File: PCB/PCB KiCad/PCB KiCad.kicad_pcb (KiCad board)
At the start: 2 copper layers, 80 x 120 mm, 0 parts

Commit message: start of component placement
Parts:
- added A1: Arduino_UNO_R3, Module:Arduino_UNO_R3, F.Cu at (71.8, 40.0)
- added C1: 100n, Capacitor_SMD:C_0805_2012Metric_Pad1.18x1.45mm_HandSolder, F.Cu at (178.0, 149.0)
- added C10: 18p, Capacitor_SMD:C_0805_2012Metric_Pad1.18x1.45mm_HandSolder, F.Cu at (64.0, 104.0)
- added C11: 10u, Capacitor_SMD:C_0805_2012Metric_Pad1.18x1.45mm_HandSolder, F.Cu at (137.0, 87.0)
- added C12: 22u, Capacitor_SMD:C_0805_2012Metric_Pad1.18x1.45mm_HandSolder, F.Cu at (134.0, 104.0)
- added C13: 100n, Capacitor_SMD:C_0805_2012Metric_Pad1.18x1.45mm_HandSolder, F.Cu at (135.0, 119.0)
- added C14: 100n, Capacitor_SMD:C_0805_2012Metric_Pad1.18x1.45mm_HandSolder, F.Cu at (136.0, 94.0)
- added C15: 100n, Capacitor_SMD:C_0805_2012Metric_Pad1.18x1.45mm_HandSolder, F.Cu at (127.0, 100.0)
- added C16: 22u, Capacitor_SMD:C_0805_2012Metric_Pad1.18x1.45mm_HandSolder, F.Cu at (127.0, 105.0)
- added C17: 100n, Capacitor_SMD:C_0805_2012Metric_Pad1.18x1.45mm_HandSolder, F.Cu at (128.0, 143.0)
- added C2: 51p, Capacitor_SMD:C_0805_2012Metric_Pad1.18x1.45mm_HandSolder, F.Cu at (196.0, 146.0)
- added C3: 51p, Capacitor_SMD:C_0805_2012Metric_Pad1.18x1.45mm_HandSolder, F.Cu at (163.0, 149.0)
- added C4: 47n, Capacitor_SMD:C_0805_2012Metric_Pad1.18x1.45mm_HandSolder, F.Cu at (171.0, 142.0)
- added C5: 100p, Capacitor_SMD:C_0805_2012Metric_Pad1.18x1.45mm_HandSolder, F.Cu at (164.0, 141.0)
- added C6: 22u, Capacitor_SMD:C_0805_2012Metric_Pad1.18x1.45mm_HandSolder, F.Cu at (199.1, 116.0)
- added C7: 100n, Capacitor_SMD:C_0805_2012Metric_Pad1.18x1.45mm_HandSolder, F.Cu at (206.0, 114.0)
- added C8: 100p, Capacitor_SMD:C_0805_2012Metric_Pad1.18x1.45mm_HandSolder, F.Cu at (215.0, 116.0)
- added C9: 18p, Capacitor_SMD:C_0805_2012Metric_Pad1.18x1.45mm_HandSolder, F.Cu at (64.0, 110.0)
- added D1: 0090-3111-185, Diode_SMD:D_1206_3216Metric_Pad1.42x1.75mm_HandSolder, F.Cu at (83.0, 161.0)
- added D10: LED, LED_SMD:LED_1206_3216Metric_Pad1.42x1.75mm_HandSolder, F.Cu at (72.5, 159.0)
- added D11: LED, LED_SMD:LED_1206_3216Metric_Pad1.42x1.75mm_HandSolder, F.Cu at (76.0, 153.0)
- added D2: LED BLUE, LED_SMD:LED_0805_2012Metric_Pad1.15x1.40mm_HandSolder, F.Cu at (79.0, 31.0)
- added D3: LED RED, LED_SMD:LED_0805_2012Metric_Pad1.15x1.40mm_HandSolder, F.Cu at (90.0, 31.0)
- added D4: LED, LED_SMD:LED_1206_3216Metric_Pad1.42x1.75mm_HandSolder, F.Cu at (90.0, 153.0)
- added D5: LED, LED_SMD:LED_1206_3216Metric_Pad1.42x1.75mm_HandSolder, F.Cu at (90.0, 159.0)
- added D6: LED, LED_SMD:LED_1206_3216Metric_Pad1.42x1.75mm_HandSolder, F.Cu at (90.0, 165.0)
- added D7: LED, LED_SMD:LED_1206_3216Metric_Pad1.42x1.75mm_HandSolder, F.Cu at (88.5, 171.0)
- added D8: LED, LED_SMD:LED_1206_3216Metric_Pad1.42x1.75mm_HandSolder, F.Cu at (74.0, 171.0)
- added D9: LED, LED_SMD:LED_1206_3216Metric_Pad1.42x1.75mm_HandSolder, F.Cu at (73.0, 165.0)
- added FB1: FerriteBead, Resistor_SMD:R_0805_2012Metric_Pad1.20x1.40mm_HandSolder, F.Cu at (128.0, 92.0)
- added J1: ADC Debug, Connector_PinHeader_2.54mm:PinHeader_1x08_P2.54mm_Vertical, F.Cu at (45.0, 101.1)
- added J2: LED Debug, Connector_PinHeader_2.54mm:PinHeader_1x04_P2.54mm_Vertical, F.Cu at (120.0, 137.0)
- added R1: 240k, Resistor_SMD:R_0805_2012Metric_Pad1.20x1.40mm_HandSolder, F.Cu at (187.0, 137.0)
- added R10: 100, Resistor_SMD:R_0805_2012Metric_Pad1.20x1.40mm_HandSolder, F.Cu at (82.7, 95.0)
- added R11: 0, Resistor_SMD:R_0805_2012Metric_Pad1.20x1.40mm_HandSolder, F.Cu at (77.3, 95.0)
- added R12: 100, Resistor_SMD:R_0805_2012Metric_Pad1.20x1.40mm_HandSolder, F.Cu at (88.1, 95.0)
- added R13: 0, Resistor_SMD:R_0805_2012Metric_Pad1.20x1.40mm_HandSolder, F.Cu at (99.0, 95.0)
- added R14: 100, Resistor_SMD:R_0805_2012Metric_Pad1.20x1.40mm_HandSolder, F.Cu at (93.6, 95.0)
- added R15: 100, Resistor_SMD:R_0805_2012Metric_Pad1.20x1.40mm_HandSolder, F.Cu at (92.0, 100.0)
- added R16: 100, Resistor_SMD:R_0805_2012Metric_Pad1.20x1.40mm_HandSolder, F.Cu at (78.0, 35.0)
- added R17: 82, Resistor_SMD:R_0805_2012Metric_Pad1.20x1.40mm_HandSolder, F.Cu at (90.0, 35.0)
- added R18: 10k, Resistor_SMD:R_0805_2012Metric_Pad1.20x1.40mm_HandSolder, F.Cu at (60.0, 23.0)
- added R19: 10k, Resistor_SMD:R_0805_2012Metric_Pad1.20x1.40mm_HandSolder, F.Cu at (73.0, 23.0)
- added R2: 240k, Resistor_SMD:R_0805_2012Metric_Pad1.20x1.40mm_HandSolder, F.Cu at (171.0, 152.0)
- added R20: 1k, Resistor_SMD:R_0805_2012Metric_Pad1.20x1.40mm_HandSolder, F.Cu at (129.0, 120.0)
- added R21: 0, Resistor_SMD:R_0805_2012Metric_Pad1.20x1.40mm_HandSolder, F.Cu at (105.0, 95.0)
- added R22: 0, Resistor_SMD:R_0805_2012Metric_Pad1.20x1.40mm_HandSolder, F.Cu at (110.0, 92.0)
- added R23: 0, Resistor_SMD:R_0805_2012Metric_Pad1.20x1.40mm_HandSolder, F.Cu at (101.0, 102.0)
- added R24: 1k, Resistor_SMD:R_0805_2012Metric_Pad1.20x1.40mm_HandSolder, F.Cu at (127.0, 149.0)
- added R25: 56, Resistor_SMD:R_0805_2012Metric_Pad1.20x1.40mm_HandSolder, F.Cu at (98.0, 153.0)
- added R26: 62, Resistor_SMD:R_0805_2012Metric_Pad1.20x1.40mm_HandSolder, F.Cu at (98.0, 159.0)
- added R27: 70, Resistor_SMD:R_0805_2012Metric_Pad1.20x1.40mm_HandSolder, F.Cu at (98.0, 165.0)
- added R28: 75, Resistor_SMD:R_0805_2012Metric_Pad1.20x1.40mm_HandSolder, F.Cu at (98.0, 171.0)
- added R29: 75, Resistor_SMD:R_0805_2012Metric_Pad1.20x1.40mm_HandSolder, F.Cu at (65.0, 171.0)
- added R3: 301, Resistor_SMD:R_0805_2012Metric_Pad1.20x1.40mm_HandSolder, F.Cu at (179.0, 139.0)
- added R30: 75, Resistor_SMD:R_0805_2012Metric_Pad1.20x1.40mm_HandSolder, F.Cu at (63.0, 165.0)
- added R31: 75, Resistor_SMD:R_0805_2012Metric_Pad1.20x1.40mm_HandSolder, F.Cu at (63.0, 159.0)
- added R32: 82, Resistor_SMD:R_0805_2012Metric_Pad1.20x1.40mm_HandSolder, F.Cu at (64.0, 153.0)
- added R4: 301, Resistor_SMD:R_0805_2012Metric_Pad1.20x1.40mm_HandSolder, F.Cu at (188.0, 147.0)
- added R5: 49.9, Resistor_SMD:R_0805_2012Metric_Pad1.20x1.40mm_HandSolder, F.Cu at (191.0, 115.0)
- added R6: 49.9, Resistor_SMD:R_0805_2012Metric_Pad1.20x1.40mm_HandSolder, F.Cu at (192.0, 121.0)
- added R7: 10k, Resistor_SMD:R_0805_2012Metric_Pad1.20x1.40mm_HandSolder, F.Cu at (61.0, 95.0)
- added R8: 10k, Resistor_SMD:R_0805_2012Metric_Pad1.20x1.40mm_HandSolder, F.Cu at (66.4, 95.0)
- added R9: 100, Resistor_SMD:R_0805_2012Metric_Pad1.20x1.40mm_HandSolder, F.Cu at (71.9, 95.0)
- added SW1: MCU_RESET, Button_Switch_THT:SW_PUSH_6mm_H4.3mm, F.Cu at (52.8, 29.8)
- added SW2: TRIGGER, Button_Switch_THT:SW_PUSH_6mm_H4.3mm, F.Cu at (63.8, 29.8)
- added U2: ADS1256IDBT, ADS1256:Texas_Instruments-ADS1256IDBT-Level_A, F.Cu at (176.5, 126.6)
- added U3: LM285D-2.5, Package_SO:SOIC-8_3.9x4.9mm_P1.27mm, F.Cu at (114.0, 121.0)
- added U4: AMS1117-3.3, Package_TO_SOT_SMD:SOT-223-3_TabPin2, F.Cu at (115.0, 102.0)
- added U5: TLC59208FIPWR, TLC59208:Texas_Instruments-TLC59208FIPWR-Level_A, F.Cu at (108.0, 142.0)
- added Y1: 7.68MHz, Crystal:Crystal_HC49-U_Vertical, F.Cu at (55.0, 110.0)

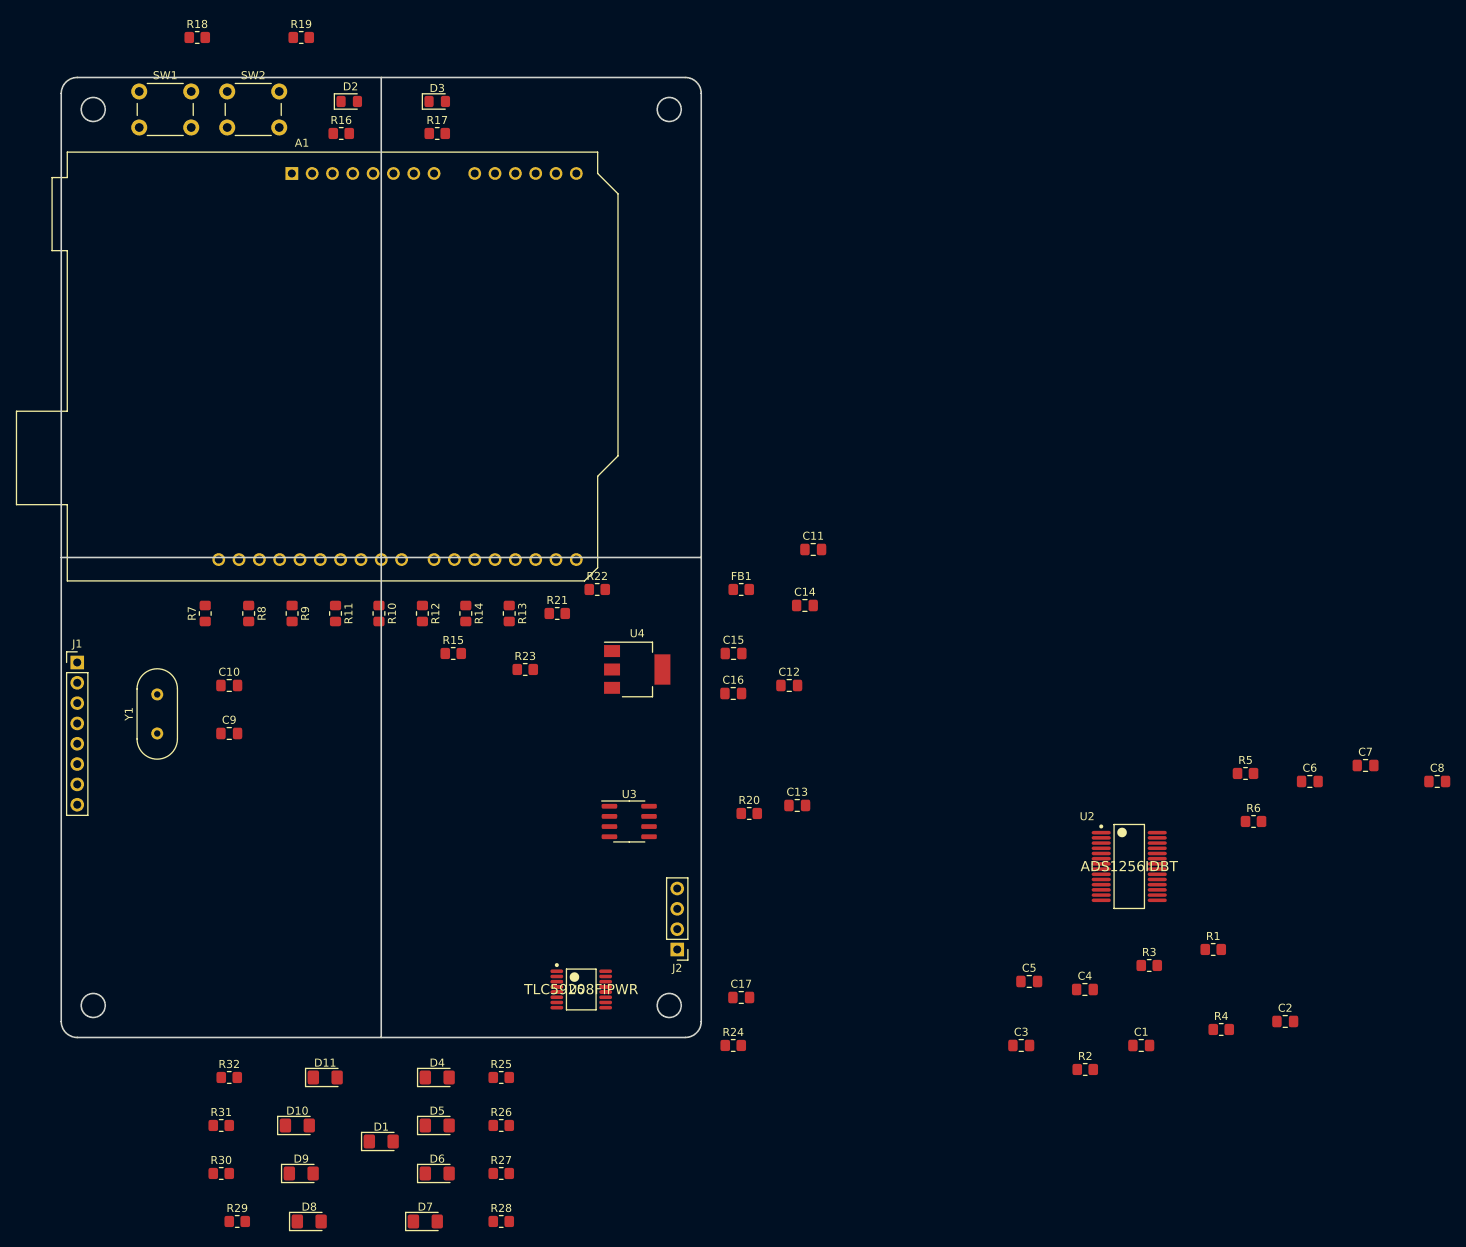
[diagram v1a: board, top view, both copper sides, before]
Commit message: placement of components
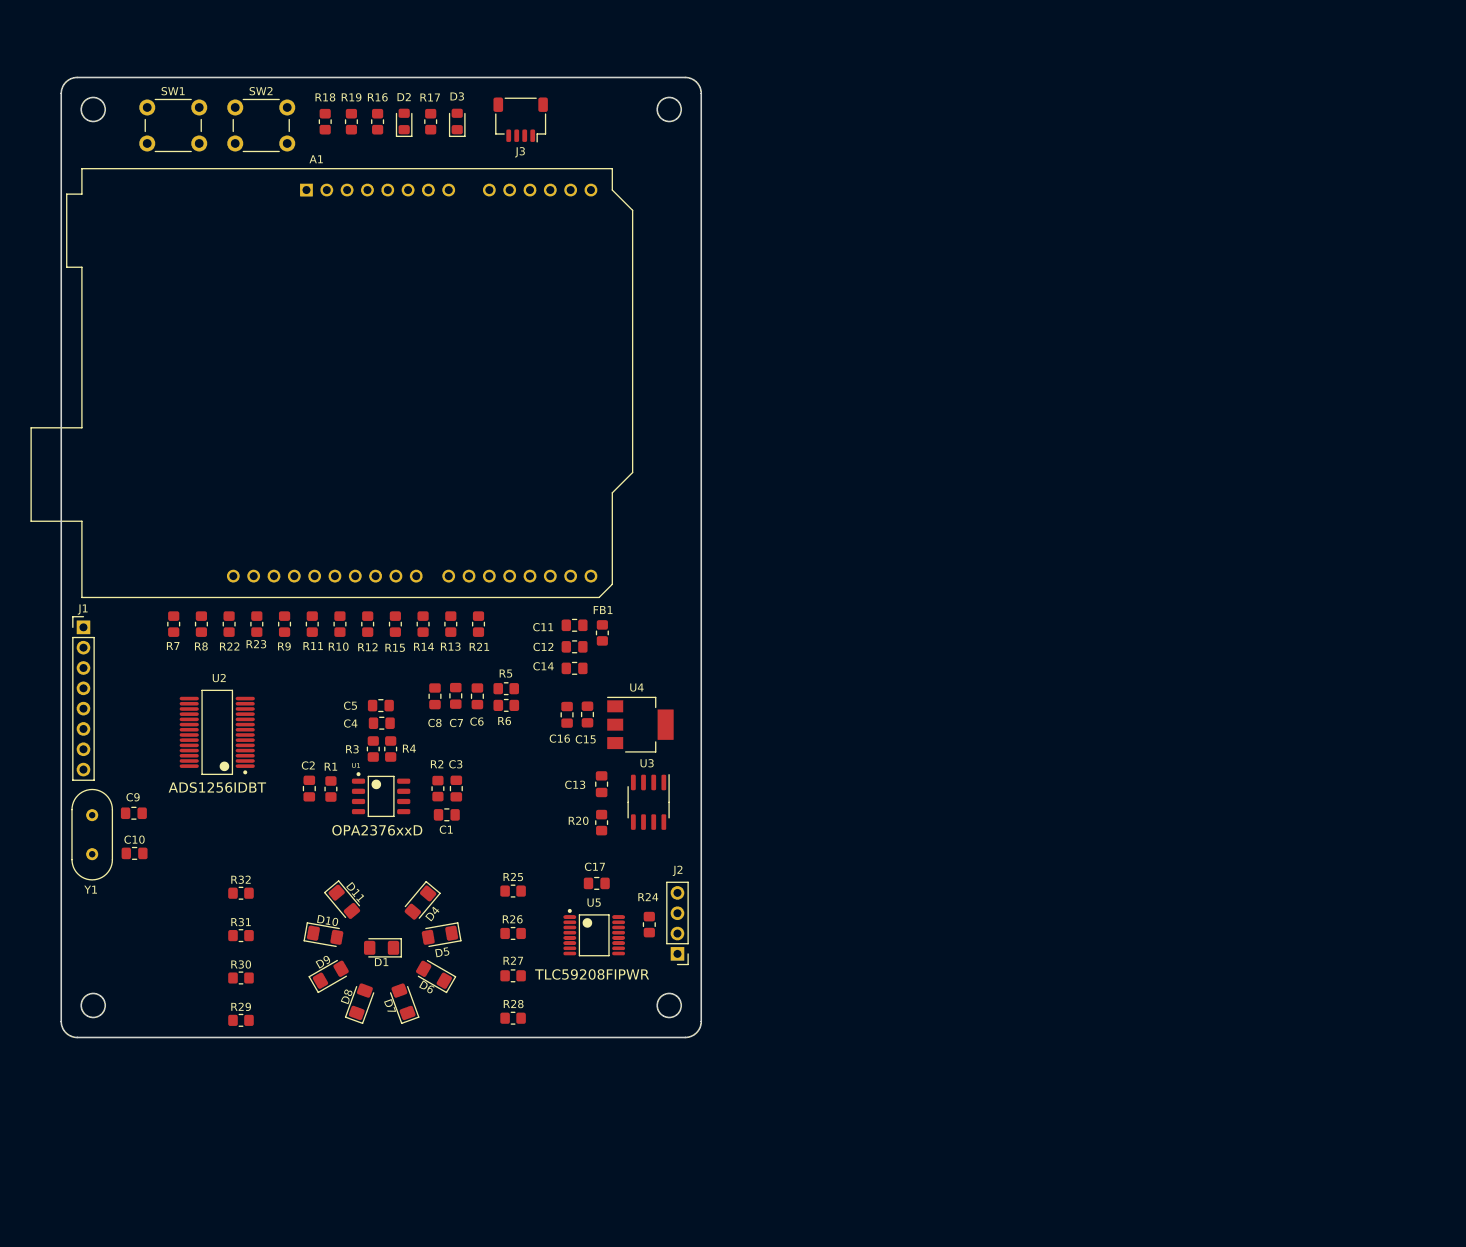
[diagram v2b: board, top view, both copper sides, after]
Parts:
- added J3: Qwiic, Connector_JST:JST_SH_SM04B-SRSS-TB_1x04-1MP_P1.00mm_Horizontal, F.Cu at (100.4, 33.3)
- added U1: OPA2376xxD, eec:Texas_Instruments-OPA2376AID-Level_A, F.Cu at (83.0, 117.9)
- SW1, SW2: footprint Button_Switch_THT:SW_PUSH_6mm_H4.3mm -> Button_Switch_THT:SW_PUSH_6mm
- moved C8 125.7 mm to (89.7, 105.3), turned to -90 degrees
- moved C2 125.4 mm to (74.0, 116.9), turned to 90 degrees
- moved U2 115.2 mm to (62.5, 109.9), turned to 180 degrees
- moved C7 114.0 mm to (92.3, 105.3), turned to -90 degrees
- moved R1 112.1 mm to (76.7, 116.9), turned to 90 degrees
- moved R4 109.6 mm to (84.2, 111.9), turned to 90 degrees
- moved C6 104.6 mm to (95.0, 105.3), turned to -90 degrees
- moved R3 100.7 mm to (82.0, 111.9), turned to 90 degrees
- moved R6 94.5 mm to (98.6, 106.5), turned to 180 degrees
- moved C4 94.0 mm to (83.1, 108.7), turned to 180 degrees
- moved R5 93.0 mm to (98.6, 104.4), turned to 180 degrees
- moved C1 91.5 mm to (91.2, 120.2), turned to 180 degrees
- moved R2 88.2 mm to (90.1, 116.9), turned to -90 degrees
- moved C5 88.1 mm to (83.0, 106.5)
- moved C3 77.6 mm to (92.4, 116.9), turned to 90 degrees
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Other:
- outline, holes or cut-outs redrawn

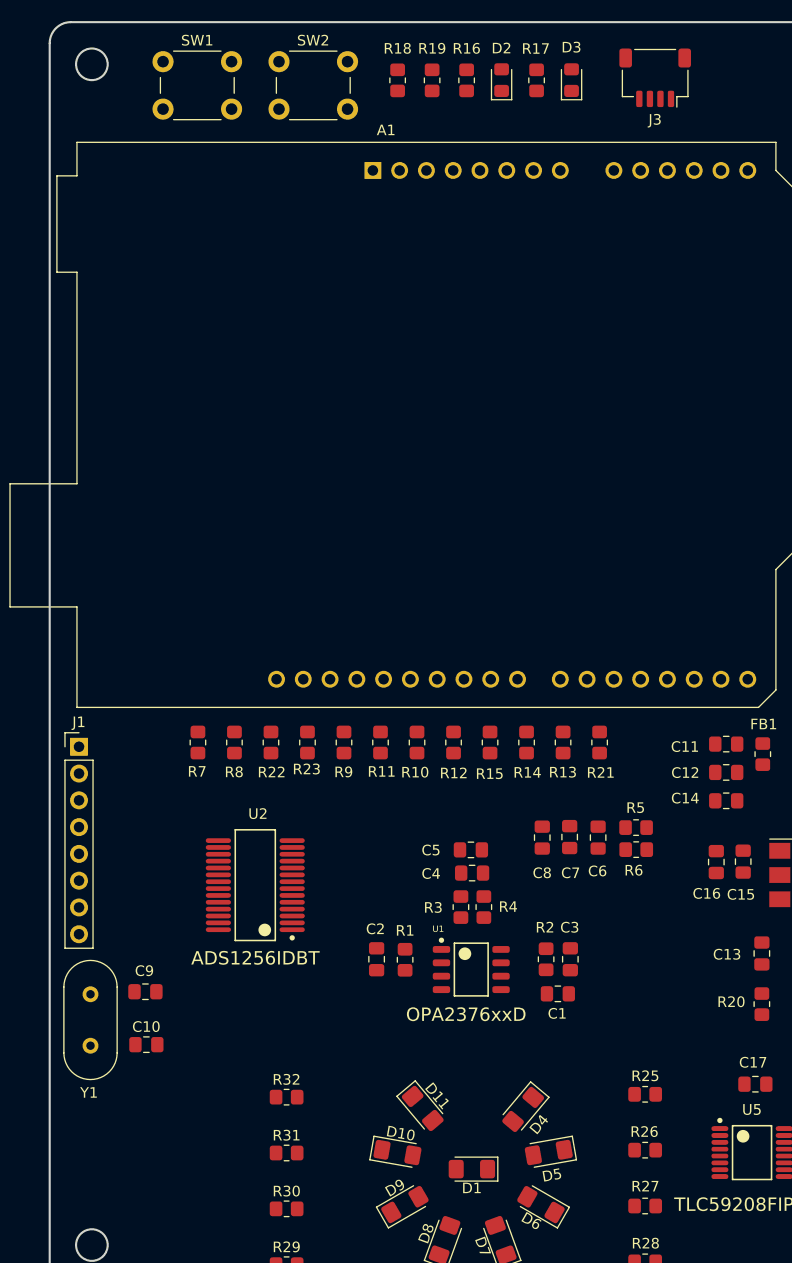
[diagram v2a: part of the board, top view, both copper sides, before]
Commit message: placement: working on the analog frontend
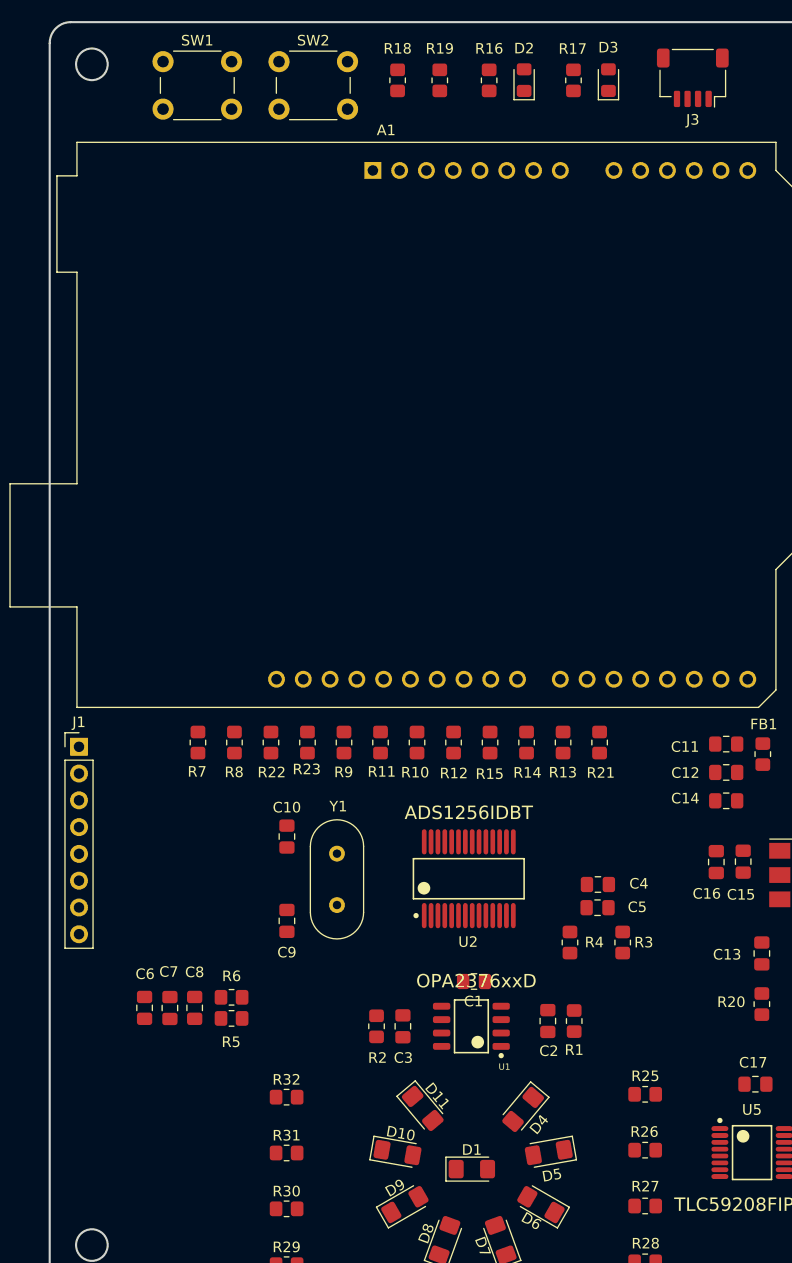
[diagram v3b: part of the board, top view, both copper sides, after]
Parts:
- moved C6 46.0 mm to (52.0, 121.5), turned to 90 degrees
- moved R5 42.4 mm to (60.2, 122.5)
- moved C7 41.2 mm to (54.4, 121.5), turned to 90 degrees
- moved R6 40.9 mm to (60.2, 120.5)
- moved C8 36.7 mm to (56.8, 121.5), turned to 90 degrees
- moved Y1 24.9 mm to (70.2, 111.8), turned to 90 degrees
- moved C10 23.8 mm to (65.5, 105.2), turned to -90 degrees
- moved U2 20.3 mm to (82.8, 109.2), turned to 90 degrees
- moved R2 17.3 mm to (74.0, 123.2), turned to 90 degrees
- moved C2 17.3 mm to (90.2, 122.8), turned to -90 degrees
- moved C3 17.1 mm to (76.5, 123.2), turned to -90 degrees
- moved R1 17.1 mm to (92.8, 122.8), turned to -90 degrees
- moved R3 15.7 mm to (97.3, 115.3)
- moved C9 15.0 mm to (65.5, 113.2), turned to -90 degrees
- moved C5 13.2 mm to (95.0, 112.0), turned to 180 degrees
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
